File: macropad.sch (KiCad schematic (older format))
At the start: 13 parts

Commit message: Power done, I think
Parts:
- added C?: 1uF, symbol Device:C_Small
- added D?: LED, symbol Device:LED
- added J?: Conn_01x02, symbol Connector_Generic:Conn_01x02
- added R?: 200, symbol Device:R_Small
- added U?: MAX1811, Package_SO:SOIC-8_3.9x4.9mm_P1.27mm, symbol Battery_Management:MAX1811
- added U?: LP5907MFX-3.3, Package_TO_SOT_SMD:SOT-23-5, symbol Regulator_Linear:LP5907MFX-3.3
- added USB?: HRO-TYPE-C-31-M-12, symbol Type-C:HRO-TYPE-C-31-M-12
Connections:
- net D+: now also R?.2, U?.4 (D+); no longer R?.1
- net D-: now also R?.2, U?.3 (D-); no longer R?.1
- net GND: now also J?.1 (Pin_1), U?.2 (GND), U?.3 (GND), U?.6 (GND), USB?.1 (GND), USB?.12 (GND), USB?.13 (SHIELD)
- net VCC: no longer U?.14 (VCC), U?.2 (UVCC), U?.24 (AVCC), U?.34 (VCC), U?.44 (AVCC), U?.7 (VBUS)
- new net: R?.1, USB?.5 (DN2), USB?.7 (DN1)
- new net: R?.1, USB?.6 (DP1), USB?.8 (DP2)
- new net: D?.1 (K), U?.8 (~CHG)
- new net: D?.2 (A), R?.1
- new net: C?.1, U?.1 (IN)
- new net BATT: C?.2, J?.2 (Pin_2), U?.5 (BATT)
- new net REG: U?.14 (VCC), U?.2 (UVCC), U?.24 (AVCC), U?.34 (VCC), U?.44 (AVCC), U?.5 (OUT)
- new net VBUS: R?.2, U?.1 (SELV), U?.2 (SELI), U?.3 (EN), U?.4 (IN), U?.7 (EN), U?.7 (VBUS), USB?.11 (VBUS), USB?.2 (VBUS)
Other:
- moved on the sheet: C?, R?, SW?, U?, Y?

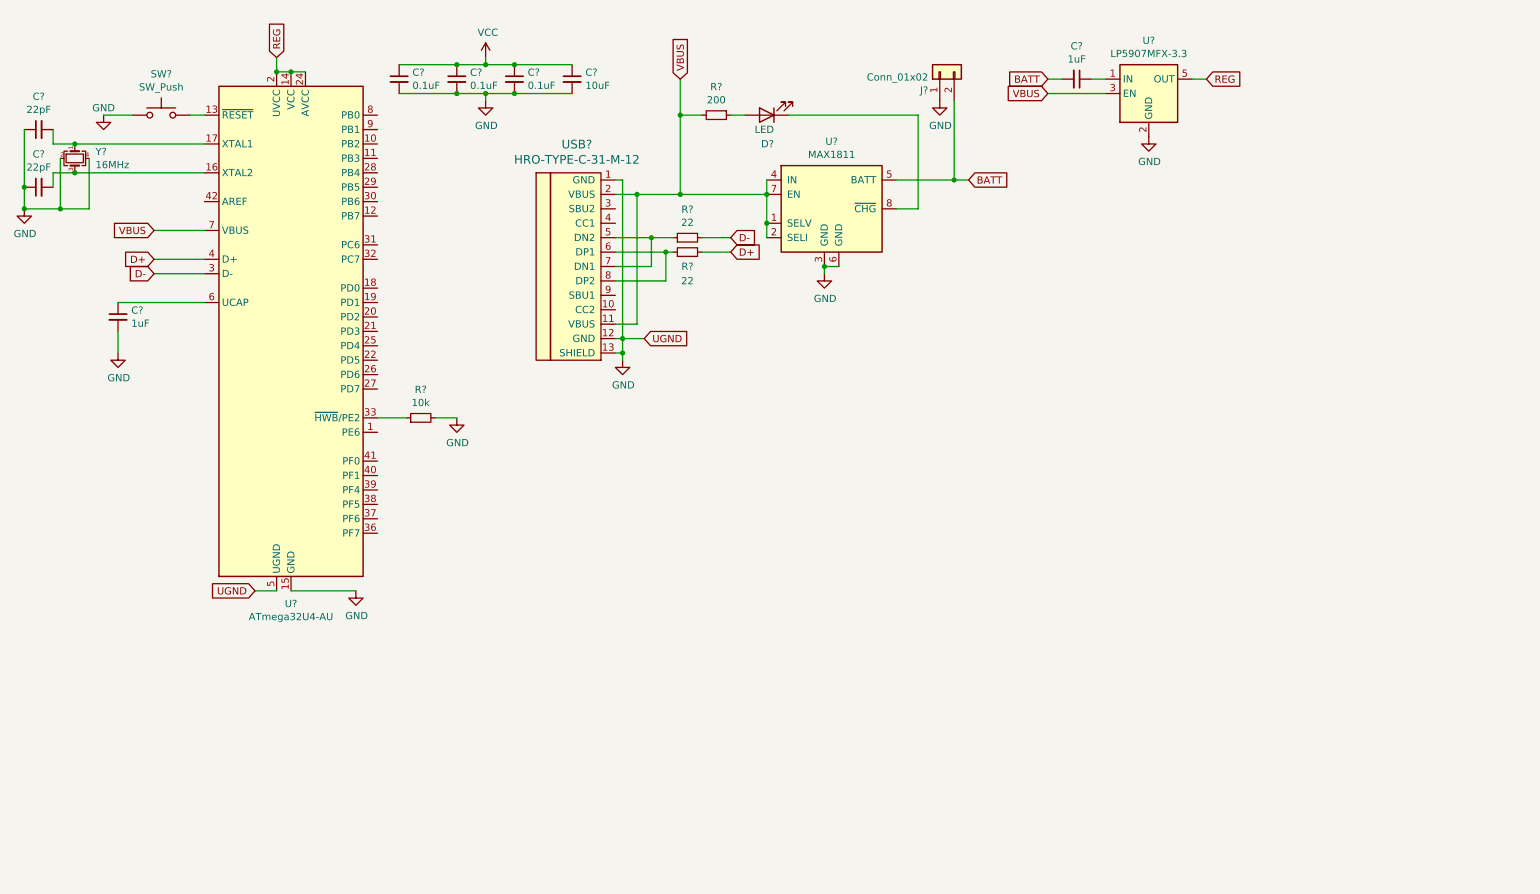
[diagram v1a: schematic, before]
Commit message: Added ESD protection + fuses
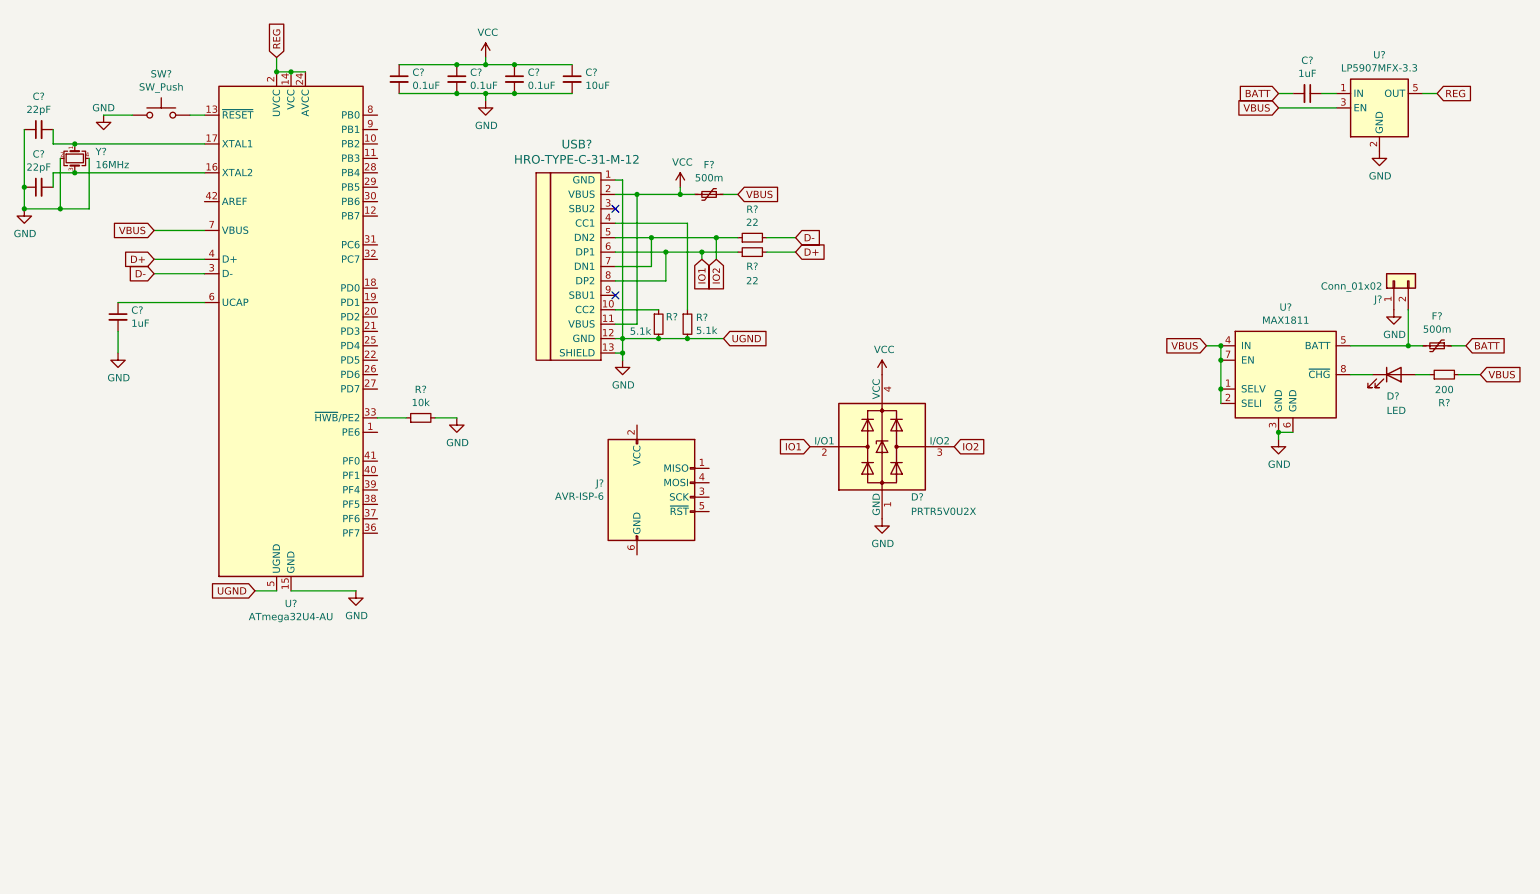
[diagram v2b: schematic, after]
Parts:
- added D?: PRTR5V0U2X, Package_TO_SOT_SMD:SOT-143, symbol Power_Protection:PRTR5V0U2X
- added F? (x2): 500m, symbol Device:Polyfuse_Small
- added J?: AVR-ISP-6, symbol Connector:AVR-ISP-6
- added R? (x2): 5.1k, symbol Device:R_Small
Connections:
- net BATT: now also F?.1; no longer J?.2 (Pin_2), U?.5 (BATT)
- net GND: now also D?.1 (GND), R?.2, R?.2
- net VBUS: now also F?.1; no longer USB?.11 (VBUS), USB?.2 (VBUS)
- net VCC: now also USB?.11 (VBUS), USB?.2 (VBUS), D?.4 (VCC), F?.2
- net IO2: now reaches R?.1, USB?.5 (DN2), USB?.7 (DN1)
- net IO2: now also D?.3 (I/O2)
- net IO1: now reaches R?.1, USB?.6 (DP1), USB?.8 (DP2)
- net IO1: now also D?.2 (I/O1)
- net at USB?.10 (CC2): now also R?.1
- net at USB?.4 (CC1): now also R?.1
- new net: F?.2, J?.2 (Pin_2), U?.5 (BATT)
- no-connect marks 0 -> 2
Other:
- moved on the sheet: C?, D?, J?, R?, U?

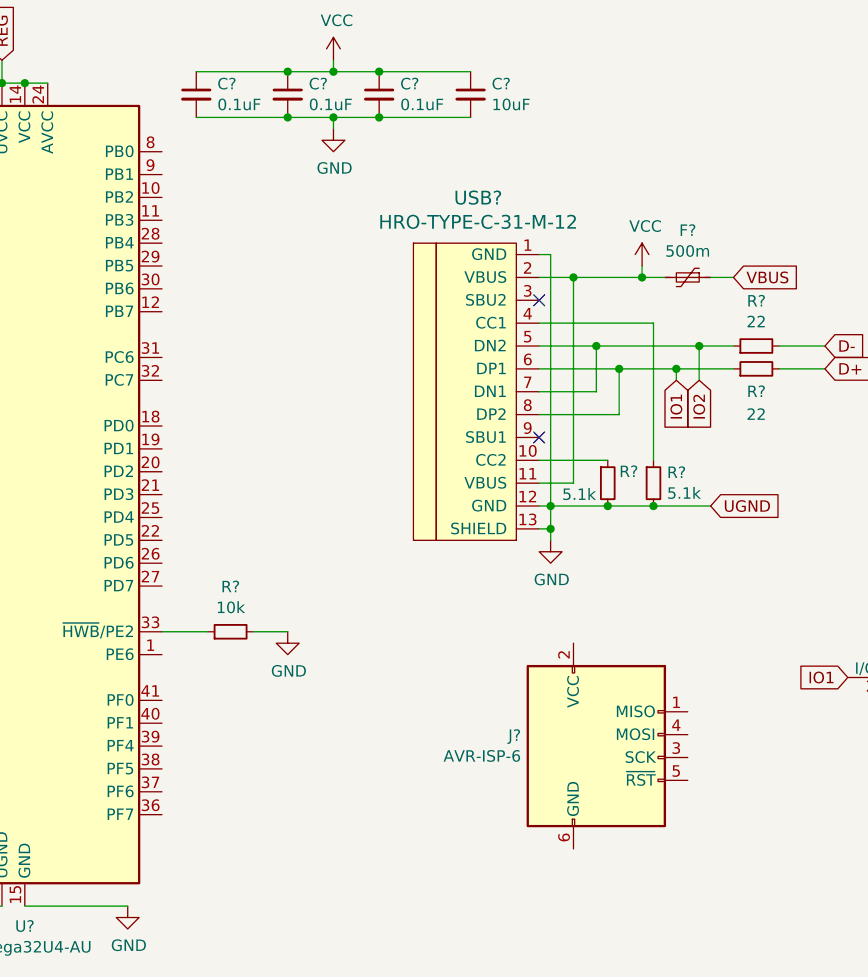
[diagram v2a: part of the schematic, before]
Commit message: Added SPI
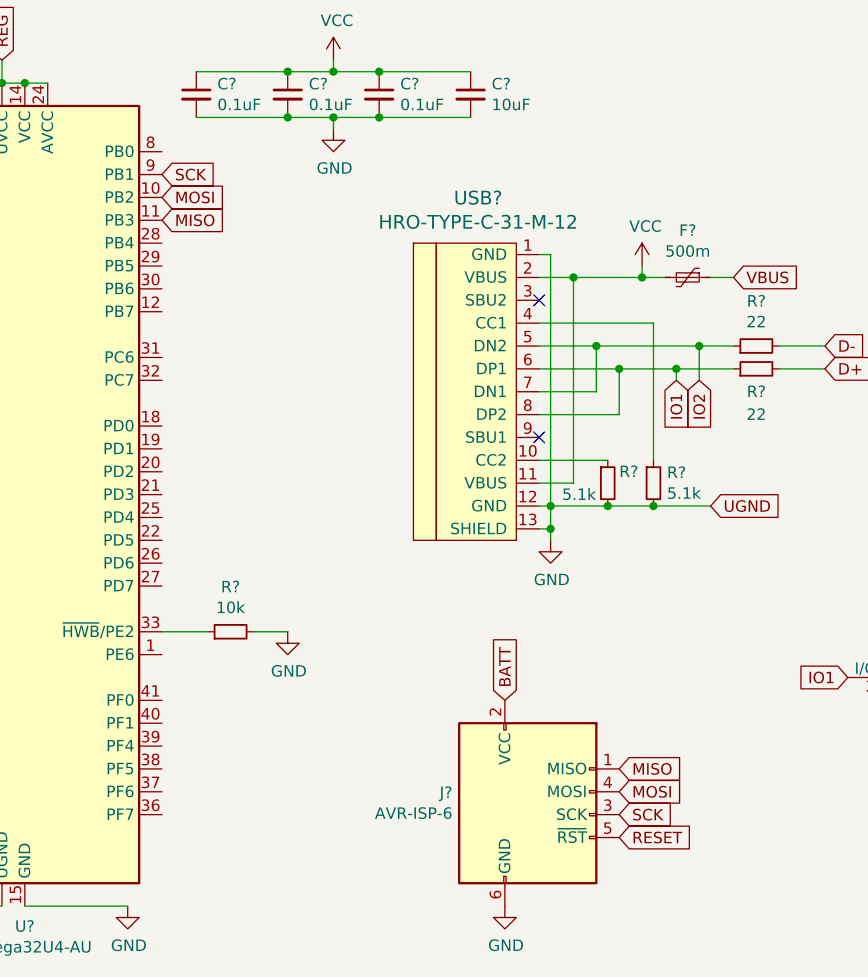
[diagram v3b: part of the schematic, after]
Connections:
- net BATT: now also J?.2 (VCC)
- net GND: now also J?.6 (GND)
- net MOSI: now reaches U?.10 (PB2)
- net MOSI: now also J?.4 (MOSI)
- net MISO: now reaches U?.11 (PB3)
- net MISO: now also J?.1 (MISO)
- net SCK: now reaches U?.9 (PB1)
- net SCK: now also J?.3 (SCK)
- net RESET: now reaches J?.5 (~RST)
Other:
- moved on the sheet: J?
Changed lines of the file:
@@
 L Connector:AVR-ISP-6 J?
 U 1 1 60E8B07C
-P 5000 3800
-F 0 "J?" H 4671 3896 50  0000 R CNN
-F 1 "AVR-ISP-6" H 4671 3805 50  0000 R CNN
-F 2 "" V 4750 3850 50  0001 C CNN
-F 3 " ~" H 3725 3250 50  0001 C CNN
-	1    5000 3800
+P 4700 4050
+F 0 "J?" H 4371 4146 50  0000 R CNN
+F 1 "AVR-ISP-6" H 4371 4055 50  0000 R CNN
+F 2 "" V 4450 4100 50  0001 C CNN
+F 3 " ~" H 3425 3500 50  0001 C CNN
+	1    4700 4050
 	1    0    0    -1
 $EndComp
@@
 Wire Wire Line
 	10650 2750 10550 2750
+Text GLabel 5100 3950 2    50   Input ~ 0
+MOSI
+Text GLabel 5100 3850 2    50   Input ~ 0
+MISO
+Text GLabel 5100 4050 2    50   Input ~ 0
+SCK
+Text GLabel 5100 4150 2    50   Input ~ 0
+RESET
+Text GLabel 4600 3550 1    50   Input ~ 0
+BATT
+$Comp
+L power:GND #PWR?
+U 1 1 60F5E9DB
+P 4600 4450
+F 0 "#PWR?" H 4600 4200 50  0001 C CNN
+F 1 "GND" H 4605 4277 50  0000 C CNN
+F 2 "" H 4600 4450 50  0001 C CNN
+F 3 "" H 4600 4450 50  0001 C CNN
+	1    4600 4450
+	1    0    0    -1
+$EndComp
+Text GLabel 3100 1250 2    50   Input ~ 0
+SCK
+Text GLabel 3100 1350 2    50   Input ~ 0
+MOSI
+Text GLabel 3100 1450 2    50   Input ~ 0
+MISO
 $EndSCHEMATC

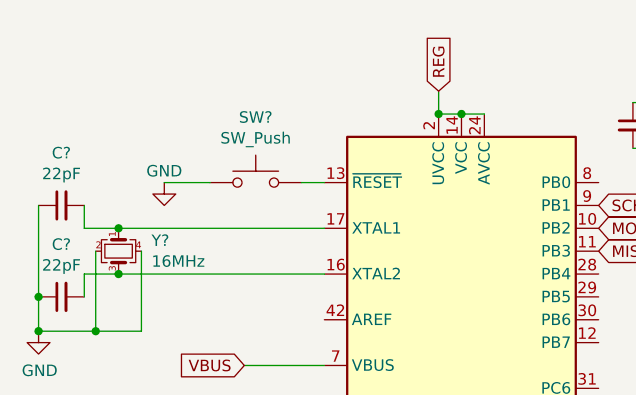
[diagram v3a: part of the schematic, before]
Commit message: Reset pull-up resistor
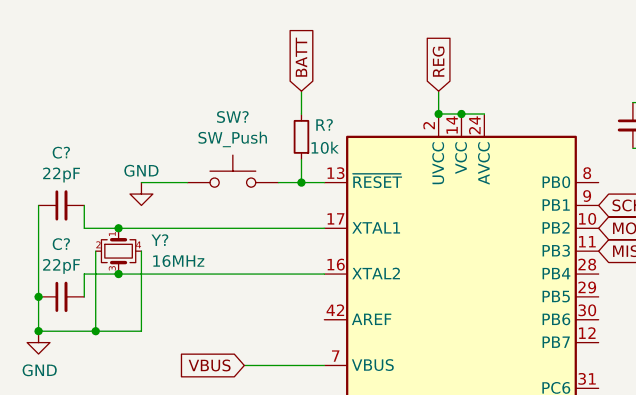
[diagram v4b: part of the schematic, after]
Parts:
- added R?: 10k, symbol Device:R_Small
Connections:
- net BATT: now also R?.2
- net at SW?.2, U?.13 (~RESET): now also R?.1
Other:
- moved on the sheet: SW?
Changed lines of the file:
@@
 L Switch:SW_Push SW?
 U 1 1 60CF57A5
-P 1600 1150
-F 0 "SW?" H 1600 1435 50  0000 C CNN
-F 1 "SW_Push" H 1600 1344 50  0000 C CNN
-F 2 "" H 1600 1350 50  0001 C CNN
-F 3 "~" H 1600 1350 50  0001 C CNN
-	1    1600 1150
-	1    0    0    -1
-$EndComp
-Wire Wire Line
-	1800 1150 1900 1150
+P 1500 1150
+F 0 "SW?" H 1500 1435 50  0000 C CNN
+F 1 "SW_Push" H 1500 1344 50  0000 C CNN
+F 2 "" H 1500 1350 50  0001 C CNN
+F 3 "~" H 1500 1350 50  0001 C CNN
+	1    1500 1150
+	1    0    0    -1
+$EndComp
 $Comp
 L power:GND #PWR?
 U 1 1 60CFD04C
-P 1200 1150
-F 0 "#PWR?" H 1200 900 50  0001 C CNN
-F 1 "GND" H 1200 1200 50  0000 C CNN
-F 2 "" H 1200 1150 50  0001 C CNN
-F 3 "" H 1200 1150 50  0001 C CNN
-	1    1200 1150
-	1    0    0    -1
-$EndComp
-Wire Wire Line
-	1200 1150 1400 1150
+P 1100 1150
+F 0 "#PWR?" H 1100 900 50  0001 C CNN
+F 1 "GND" H 1100 1200 50  0000 C CNN
+F 2 "" H 1100 1150 50  0001 C CNN
+F 3 "" H 1100 1150 50  0001 C CNN
+	1    1100 1150
+	1    0    0    -1
+$EndComp
+Wire Wire Line
+	1100 1150 1300 1150
 $Comp
 L Type-C:HRO-TYPE-C-31-M-12 USB?
@@
 Text GLabel 3100 1450 2    50   Input ~ 0
 MISO
+Wire Wire Line
+	1700 1150 1800 1150
+Text GLabel 1800 750  1    50   Input ~ 0
+BATT
+Wire Wire Line
+	1800 750  1800 850
+Wire Wire Line
+	1800 1050 1800 1150
+Connection ~ 1800 1150
+Wire Wire Line
+	1800 1150 1900 1150
+$Comp
+L Device:R_Small R?
+U 1 1 60F700A9
+P 1800 950
+F 0 "R?" H 1700 900 50  0000 C CNN
+F 1 "10k" H 1700 1000 50  0000 C CNN
+F 2 "" H 1800 950 50  0001 C CNN
+F 3 "~" H 1800 950 50  0001 C CNN
+	1    1800 950
+	-1   0    0    1
+$EndComp
 $EndSCHEMATC
